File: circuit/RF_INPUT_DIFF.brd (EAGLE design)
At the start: 64.4 x 80 mm, 100 parts, among them IC1 TS464, IC4 TS462D, IC5 TS462D, IC6 TS462D, IC7 4052D, Q1 IRML6302, Q2 IRML6302, Q3 2N7002, U1 SA612, U2 SA612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

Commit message: - продолжили работу над diff входом
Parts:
- removed C30: nc, rcl:C0805
- removed C36: 100N, rcl:C0603
- removed C9: 100n, rcl:C0603
- removed IC7: 4052D, 40xx:SO16
- added IC2: SN74LVC1G3157DBVR, balmer:SOT23-6
- added R49, R51: 220, rcl:R0603
- added R50: 22K, rcl:R0603
- added X2: (no value), con-phoenix-254:6POL254
- IC1: value TS464 -> SN74LVC1G3157DBVR; device linear:SO14 -> balmer:SOT23-6
- R24: value 330K -> 4.7K
- R25, R26: value 4K7 -> 330K
- R39: value 22K -> 150K
- R41: value 330k -> 22K
- R5: value 330K -> 15K
- R6, R9: value 15K -> 330K
- moved IC1 134.5 mm to (-37.5, -62.2), turned to 0 degrees
- moved R41 130.0 mm to (-33.7, -52.1), turned to 0 degrees
- moved R39 87.6 mm to (-33.7, -47.0)
- renumbered X4 to RX, X6 to TX
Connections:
- net ADC_REF_M renamed REF_B
- net ADC_REF_P renamed REF_A
- removed net ADC_SWITCH_NO: C30.1, IC1.8, R37.2
- removed net N$41: C30.2, IC1.9, R37.1, R38.2
- removed net N$43: C31.1, R38.1
- removed net N$44: C32.1, R39.1
- removed net N$46: IC1.13, IC1.14
- removed net N$47: IC1.10, R39.2, R41.1
- removed net V+: IC4.8, IC5.8, IC6.8
- removed net V-: IC4.4, IC5.4, IC6.4
- removed net VCC: IC7.16
- removed net VEE: IC7.7
- new net N$11: C31.1, IC6.3, R41.1
- new net N$12: C32.1, IC6.5, R50.2
- new net N$2: IC6.2, R37.1, R38.1
- new net N$25: IC6.1, R37.2, R45.1
- new net N$26: IC6.6, R38.2, R39.1
- new net N$27: IC6.7, R39.2, R51.1
- new net RX_A: IC1.1, R49.2
- new net RX_B: IC2.1, R36.2
- new net TX_A: IC1.3, R51.2
- new net TX_B: IC2.3, R45.2
- net +6V0: now also IC1.5, IC2.5, IC4.8, IC5.8, IC6.8; no longer C9.1, IC1.4
- net GND: now also IC1.2, IC2.2, IC4.4, IC5.4, IC6.4; no longer C36.2, C9.2, IC1.11, IC1.12, IC7.8
- net N$23: now also R36.1
- net N$24: now also R49.1
- net OPA_BIAS: now also R50.1; no longer C36.1
- net SET_CHANNEL: now also IC1.6, IC2.6
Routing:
- net N$41: track 58.6 -> 0.00 mm, vias 2 -> 0
- net N$47: track 49.0 -> 0.00 mm, vias 2 -> 0
- net GND: track 383.9 -> 374.8 mm
- net OPA_BIAS: track 40.8 -> 32.5 mm
- net ADC_SWITCH_NO: track 6.46 -> 0.00 mm
- net +6V0: track 211.5 -> 208.1 mm
- net N$44: track 3.28 -> 0.00 mm
- net N$43: track 3.28 -> 0.00 mm
- net N$46: track 1.27 -> 0.00 mm

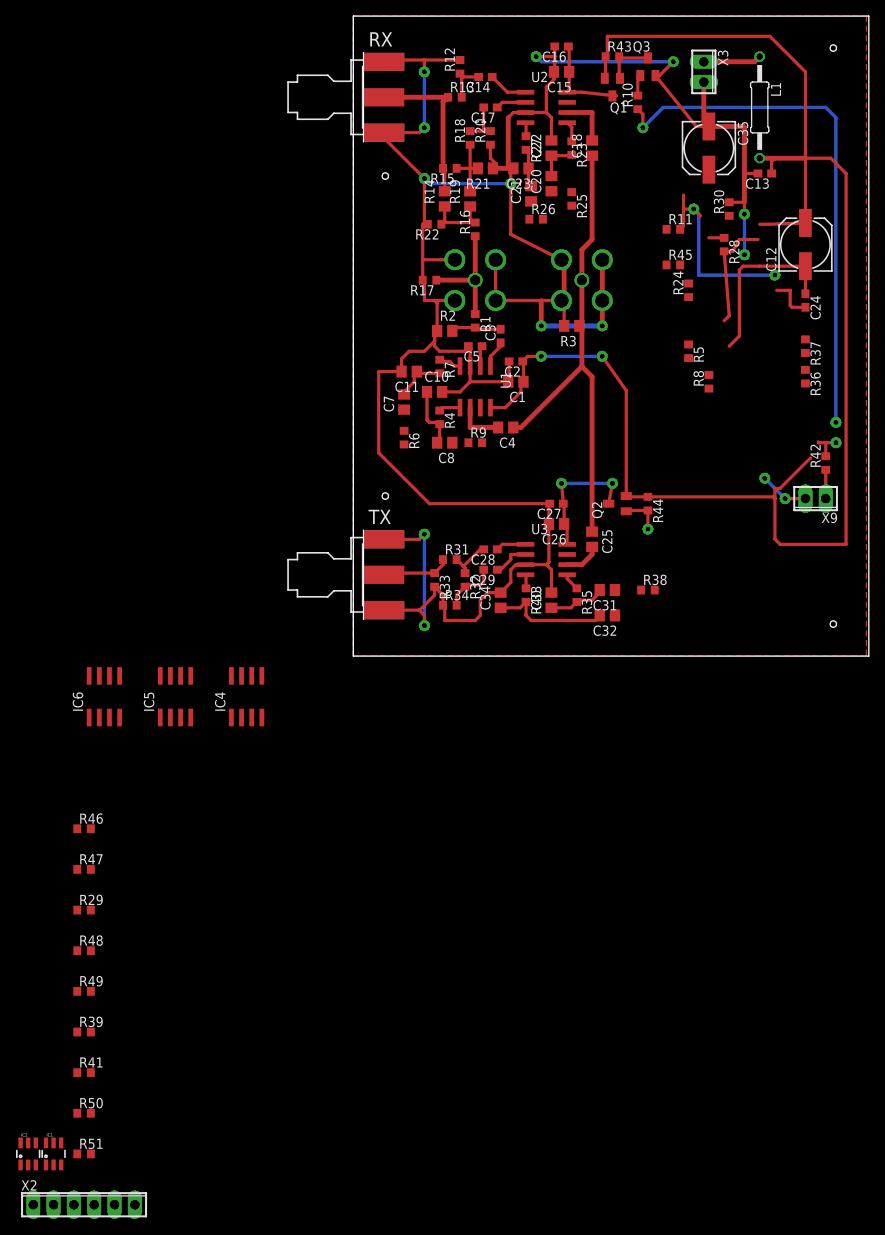
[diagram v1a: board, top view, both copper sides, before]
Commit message: - начали рисовать платку для diff выхода.
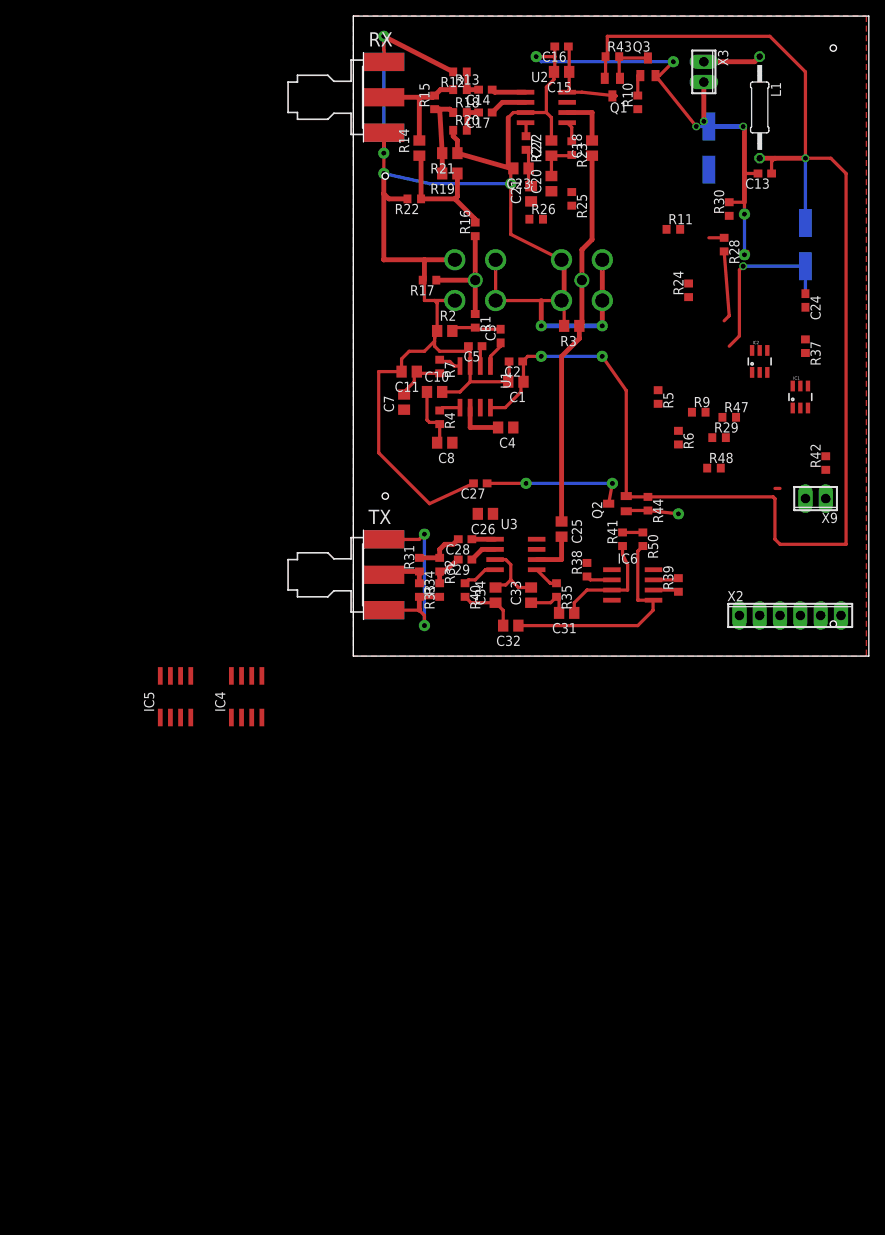
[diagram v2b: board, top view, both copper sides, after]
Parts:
- removed R36, R45, R46, R49, R51, R8: 220, rcl:R0603
- C10, C11, C22, C23, C33, C34: value 1N -> 10N
- moved IC2 134.8 mm to (50.8, 36.8)
- moved IC1 132.9 mm to (55.9, 32.4)
- moved X2 115.0 mm to (54.6, 5.08)
- moved R50 100.1 mm to (36.2, 14.6), turned to 270 degrees
- moved R48 99.2 mm to (45.1, 23.5)
- moved R29 98.9 mm to (45.7, 27.3)
- moved R47 98.5 mm to (47.0, 29.8)
- moved R41 94.7 mm to (33.7, 14.6), turned to 90 degrees
- moved R39 93.0 mm to (40.6, 8.89), turned to 90 degrees
- moved IC6 67.5 mm to (34.9, 8.89), turned to 270 degrees
- moved R6 34.3 mm to (40.6, 27.3)
- moved R9 28.2 mm to (43.2, 30.5)
- moved C32 12.1 mm to (19.7, 3.81)
- moved C27 9.86 mm to (15.9, 21.6)
- moved C26 8.98 mm to (16.5, 17.8)
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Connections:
- removed net N$15: IC4.1, R6.2, R8.2
- removed net N$16: IC4.7, R46.2, R9.2
- removed net N$23: IC5.1, R25.2, R36.1
- removed net N$24: IC5.7, R26.2, R49.1
- removed net N$25: IC6.1, R37.2, R45.1
- removed net N$27: IC6.7, R39.2, R51.1
- new net ADC_A: IC1.4, X2.4
- new net ADC_B: IC2.4, X2.5
- net GND: now also X2.1, X2.6
- net REF_A: now also IC4.1, R6.2, X2.3; no longer R8.1
- net REF_B: now also IC4.7, R9.2, X2.2; no longer R46.1
- net RX_A: now also IC5.7, R26.2; no longer R49.2
- net RX_B: now also IC5.1, R25.2; no longer R36.2
- net TX_A: now also IC6.7, R39.2; no longer R51.2
- net TX_B: now also IC6.1, R37.2; no longer R45.2
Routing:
- net SET_CHANNEL: track 75.6 -> 6.58 mm, vias 4 -> 1
- net OPA_BIAS: track 32.5 -> 4.44 mm, vias 2 -> 0
- net N$12: track 0.00 -> 27.9 mm
- net GND: track 374.8 -> 357.2 mm, vias 14 -> 16
- net +6V0: track 208.1 -> 190.7 mm, vias 2 -> 3
- net N$11: track 0.00 -> 14.2 mm
- net LO_TX: track 60.0 -> 47.3 mm
- net N$63: track 8.85 -> 17.0 mm
- net N$37: track 14.9 -> 7.37 mm
- net N$5: track 20.2 -> 14.4 mm
- net N$9: track 3.60 -> 0.00 mm
- net N$2: track 0.00 -> 3.29 mm
- net N$26: track 0.00 -> 3.20 mm
- net TX_A: track 0.00 -> 3.20 mm
- net N$36: track 1.71 -> 4.45 mm
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
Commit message: - еще немного развели плату
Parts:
- moved IC5 87.1 mm to (38.7, 57.1), turned to 90 degrees
- moved IC4 63.6 mm to (39.4, 30.5), turned to 90 degrees
- moved R48 39.4 mm to (38.1, 62.2), turned to 270 degrees
- moved R37 38.6 mm to (29.8, 10.8), turned to 90 degrees
- moved R29 34.3 mm to (43.8, 61.6)
- moved C24 31.0 mm to (38.7, 69.8), flipped to the bottom
- moved X2 28.9 mm to (59.1, 33.7), flipped to the bottom, turned to 90 degrees
- moved R11 18.4 mm to (40.6, 34.9), turned to 90 degrees
- moved R24 17.9 mm to (33.7, 61.6), turned to 270 degrees
- moved R25 16.6 mm to (43.8, 55.9)
- moved R47 11.4 mm to (36.8, 34.9), turned to 270 degrees
- moved X3 11.3 mm to (54.6, 69.8)
- moved R26 11.1 mm to (33.7, 57.1), turned to 270 degrees
- moved R9 10.2 mm to (33.0, 30.5), turned to 270 degrees
- moved C35 7.65 mm to (43.8, 71.1)
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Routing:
- net GND: track 357.2 -> 470.0 mm
- net OPA_BIAS: track 4.44 -> 103.8 mm, vias 0 -> 3
- net TX_B: track 0.00 -> 53.9 mm, vias 0 -> 2
- net N$17: track 0.00 -> 53.9 mm, vias 0 -> 2
- net +6V0: track 190.7 -> 242.5 mm
- net TX_A: track 3.20 -> 38.4 mm, vias 0 -> 2
- net N$18: track 0.00 -> 35.0 mm, vias 0 -> 2
- net N$10: track 0.00 -> 32.9 mm, vias 0 -> 2
- net REF_B: track 0.00 -> 32.0 mm
- net N$19: track 0.00 -> 27.5 mm, vias 0 -> 2
- net N$20: track 0.00 -> 26.1 mm, vias 0 -> 2
- net N$26: track 3.20 -> 24.2 mm, vias 0 -> 2
- net REF_A: track 0.00 -> 18.8 mm
- net SET_CHANNEL: track 6.58 -> 25.1 mm, vias 1 -> 3
- net N$13: track 0.00 -> 6.52 mm
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
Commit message: - начали калибровку по S параметрам
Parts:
- moved R24 11.1 mm to (39.4, 52.1), turned to 180 degrees
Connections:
- net +6V0: no longer IC5.8, IC6.8
- net N$4: now also IC6.8
- net N$8: now also IC5.8
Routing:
- net +6V0: track 242.5 -> 205.6 mm, vias 3 -> 5
- net GND: track 470.0 -> 504.3 mm, vias 16 -> 17
- net RX_A: track 2.57 -> 34.1 mm, vias 0 -> 2
- net SET_CHANNEL: track 25.1 -> 44.9 mm
- net N$4: track 22.0 -> 41.6 mm
- net N$8: track 12.5 -> 31.9 mm
- net RX_B: track 2.57 -> 21.7 mm, vias 0 -> 2
- net N$22: track 2.57 -> 8.80 mm
- net N$21: track 5.31 -> 10.6 mm
- net OPA_BIAS: track 103.8 -> 105.4 mm
- net TX_B: track 53.9 -> 54.8 mm
